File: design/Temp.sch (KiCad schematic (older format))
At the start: 3 parts

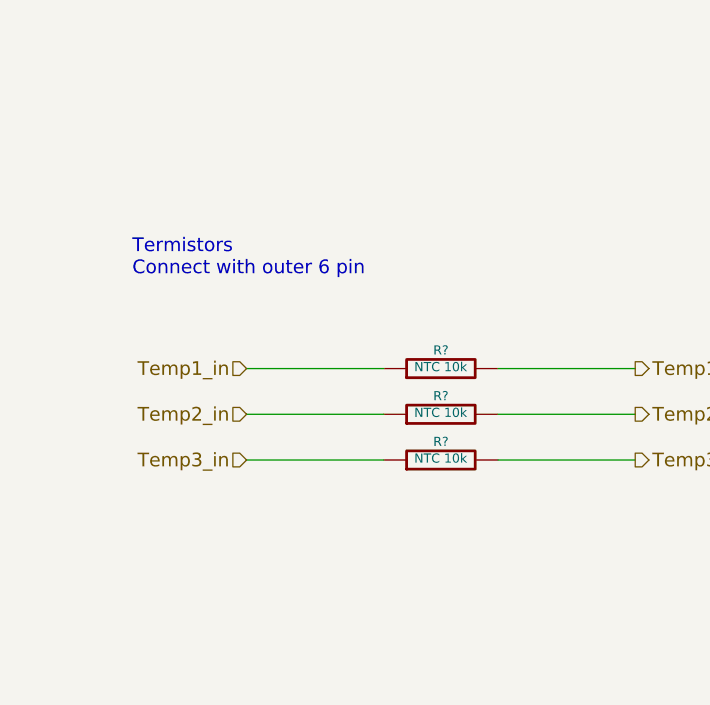
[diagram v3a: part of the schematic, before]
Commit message: Fix some schematic update pdf
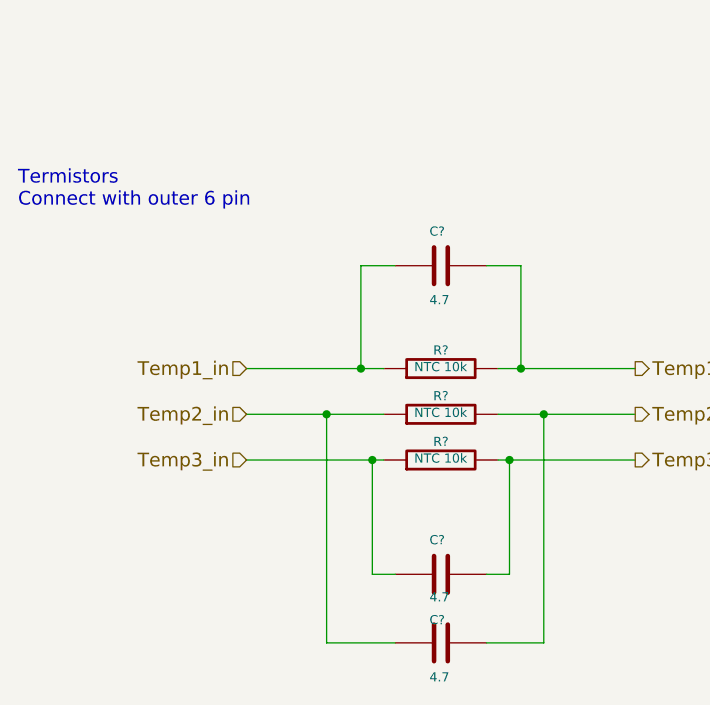
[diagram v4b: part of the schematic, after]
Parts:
- added C? (x3): 4.7, symbol C
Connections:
- net Temp1_in: now also C?.2
- net Temp1_out: now also C?.1
- net Temp2_in: now also C?.2
- net Temp2_out: now also C?.1
- net Temp3_in: now also C?.2
- net Temp3_out: now also C?.1
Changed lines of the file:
@@
 U 1 1 55845069
 P 4500 2350
+AR Path="/55BB8FBC/55844E2F/55845069" Ref="R?"  Part="1"
+AR Path="/55C14E4B/55844E2F/55845069" Ref="R?"  Part="1"
 F 0 "R?" V 4580 2350 40  0000 C CNN
 F 1 "NTC 10k" V 4507 2351 40  0000 C CNN
@@
 U 1 1 558451B7
 P 4500 2550
+AR Path="/55BB8FBC/55844E2F/558451B7" Ref="R?"  Part="1"
+AR Path="/55C14E4B/55844E2F/558451B7" Ref="R?"  Part="1"
 F 0 "R?" V 4580 2550 40  0000 C CNN
 F 1 "NTC 10k" V 4507 2551 40  0000 C CNN
@@
 U 1 1 558451FF
 P 4500 2750
+AR Path="/55BB8FBC/55844E2F/558451FF" Ref="R?"  Part="1"
+AR Path="/55C14E4B/55844E2F/558451FF" Ref="R?"  Part="1"
 F 0 "R?" V 4580 2750 40  0000 C CNN
 F 1 "NTC 10k" V 4507 2751 40  0000 C CNN
@@
 Text HLabel 3650 2750 0    60   Input ~ 0
 Temp3_in
-Wire Wire Line
-	3650 2350 4250 2350
-Wire Wire Line
-	3650 2550 4250 2550
-Wire Wire Line
-	3650 2750 4250 2750
 Text HLabel 5350 2350 2    60   Output ~ 0
 Temp1_out
@@
 Text HLabel 5350 2750 2    60   Output ~ 0
 Temp3_out
-Wire Wire Line
-	4750 2750 5350 2750
-Wire Wire Line
-	5350 2550 4750 2550
-Wire Wire Line
-	4750 2350 5350 2350
-Text Notes 3150 1950 0    60   ~ 0
+Text Notes 2650 1650 0    60   ~ 0
 Termistors\nConnect with outer 6 pin
 $Bitmap
@@
 82 20 08 82 20 08 82 20 08 82 20 08 82 20 08 82 20 08 82 20 08 82 20 08 82 20 08 82 20 08 82 20
 08 82 20 08 82 20 08 82 20 08 82 20 08 82 20 08 62 42 FE 1F B4 B0 EA B8 71 1B 11 2A 00 00 00 00
-49 45 4E 44 AE 42 60 82 80
+49 45 4E 44 AE 42 60 82 F0
 EndData
 $EndBitmap
 Text Notes 9850 800  2    60   ~ 0
 Missing only for NTC so we can convert to Temp
+$Comp
+L C C?
+U 1 1 55DF2E2F
+P 4500 3250
+F 0 "C?" V 4350 3200 40  0000 L CNN
+F 1 "4.7" V 4600 3200 40  0000 L CNN
+F 2 "" H 4538 3100 30  0000 C CNN
+F 3 "" H 4500 3250 60  0000 C CNN
+	1    4500 3250
+	0    1    1    0
+$EndComp
+$Comp
+L C C?
+U 1 1 55DF2F28
+P 4500 3550
+F 0 "C?" V 4400 3500 40  0000 L CNN
+F 1 "4.7" V 4650 3500 40  0000 L CNN
+F 2 "" H 4538 3400 30  0000 C CNN
+F 3 "" H 4500 3550 60  0000 C CNN
+	1    4500 3550
+	0    1    1    0
+$EndComp
+$Comp
+L C C?
+U 1 1 55DF2F5C
+P 4500 1900
+F 0 "C?" V 4350 1850 40  0000 L CNN
+F 1 "4.7" V 4650 1850 40  0000 L CNN
+F 2 "" H 4538 1750 30  0000 C CNN
+F 3 "" H 4500 1900 60  0000 C CNN
+	1    4500 1900
+	0    1    1    0
+$EndComp
+Wire Wire Line
+	3650 2350 4250 2350
+Wire Wire Line
+	3650 2550 4250 2550
+Wire Wire Line
+	3650 2750 4250 2750
+Wire Wire Line
+	4750 2750 5350 2750
+Wire Wire Line
+	5350 2550 4750 2550
+Wire Wire Line
+	4750 2350 5350 2350
+Wire Wire Line
+	4300 3250 4200 3250
+Wire Wire Line
+	4200 3250 4200 2750
+Connection ~ 4200 2750
+Wire Wire Line
+	4800 3250 4800 2750
+Connection ~ 4800 2750
+Wire Wire Line
+	4300 3550 4000 3550
+Wire Wire Line
+	4000 3550 4000 2550
+Connection ~ 4000 2550
+Wire Wire Line
+	4700 3550 4950 3550
+Wire Wire Line
+	4950 3550 4950 2550
+Connection ~ 4950 2550
+Wire Wire Line
+	4300 1900 4150 1900
+Wire Wire Line
+	4150 1900 4150 2350
+Connection ~ 4150 2350
+Wire Wire Line
+	4700 1900 4850 1900
+Wire Wire Line
+	4850 1900 4850 2350
+Connection ~ 4850 2350
+Wire Wire Line
+	4700 3250 4800 3250
 $EndSCHEMATC
